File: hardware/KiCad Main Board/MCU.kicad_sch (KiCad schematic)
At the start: 41 parts, among them J1 SWD Debug, J2 USB_C_Receptacle_USB2.0_14P, U1 W25Q128JVS, U7 RP2350B-QFN80, Y1 ABM8-272-T3

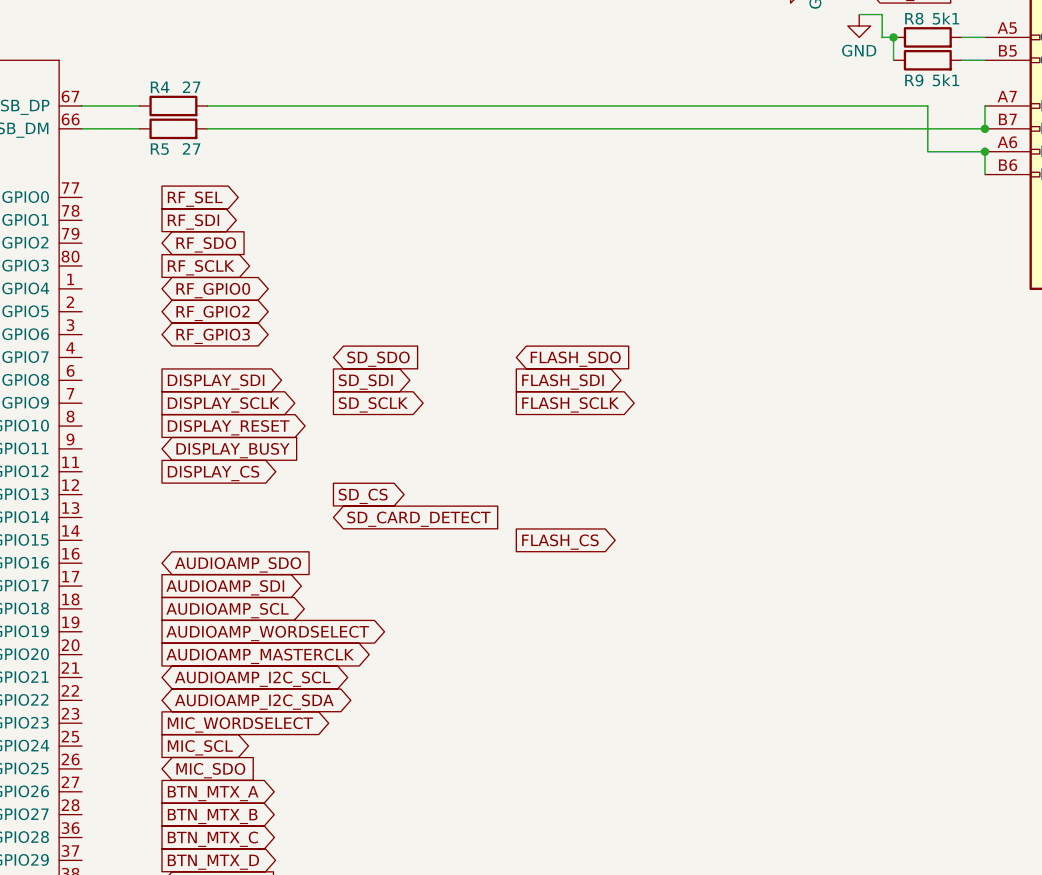
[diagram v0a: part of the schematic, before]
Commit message: added connector for RF daughter board
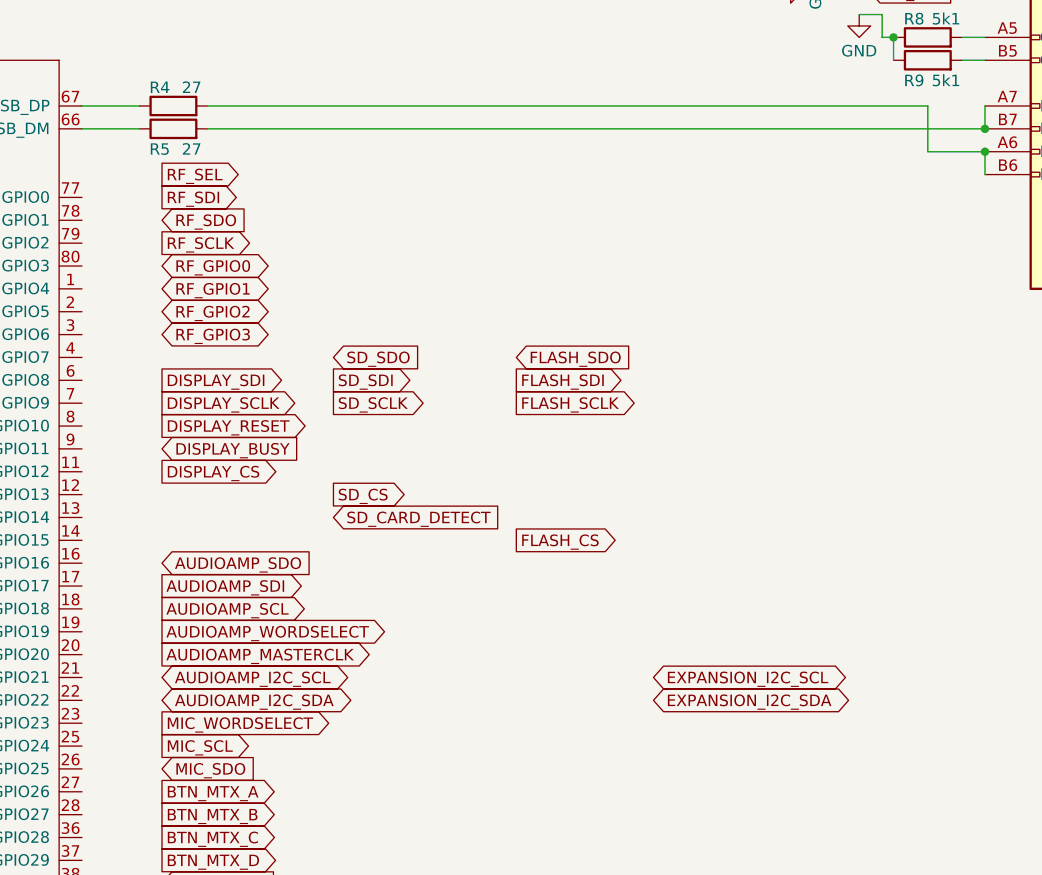
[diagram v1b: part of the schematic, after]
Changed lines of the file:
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@@
 				)
 			)
-			(table_cell "CC1120 (RF IC), Wisblock GPS/Expansions"
+			(table_cell "CC1120 (RF IC), Expansion"
 				(exclude_from_sim no)
 				(at 218.44 143.51 0)
@@
 				)
 			)
-			(table_cell "Audio IC, Wisblock GPS/Expansions"
+			(table_cell "Audio IC, Expansion"
 				(exclude_from_sim no)
 				(at 218.44 148.59 0)
@@
 		)
 	)
+	(global_label "RF_GPIO1"
+		(shape bidirectional)
+		(at 156.21 63.5 0)
+		(fields_autoplaced yes)
+		(effects
+			(font
+				(size 1.27 1.27)
+			)
+			(justify left)
+		)
+		(property "Intersheetrefs" "${INTERSHEET_REFS}"
+			(at 169.3175 63.5 0)
+			(effects
+				(font
+					(size 1.27 1.27)
+				)
+				(justify left)
+				(hide yes)
+			)
+		)
+	)
 	(global_label "BTN_MTX_3"
 		(shape input)
@@
 	(global_label "RF_SDO"
 		(shape input)
-		(at 156.21 58.42 0)
-		(fields_autoplaced yes)
-		(effects
-			(font
-				(size 1.27 1.27)
-			)
-			(justify left)
-		)
-		(property "Intersheetrefs" "${INTERSHEET_REFS}"
-			(at 166.3314 58.42 0)
+		(at 156.21 55.88 0)
+		(fields_autoplaced yes)
+		(effects
+			(font
+				(size 1.27 1.27)
+			)
+			(justify left)
+		)
+		(property "Intersheetrefs" "${INTERSHEET_REFS}"
+			(at 166.3314 55.88 0)
 			(effects
 				(font
@@
 		)
 	)
+	(global_label "EXPANSION_I2C_SCL"
+		(shape bidirectional)
+		(at 210.82 106.68 0)
+		(fields_autoplaced yes)
+		(effects
+			(font
+				(size 1.27 1.27)
+			)
+			(justify left)
+		)
+		(property "Intersheetrefs" "${INTERSHEET_REFS}"
+			(at 233.9665 106.68 0)
+			(effects
+				(font
+					(size 1.27 1.27)
+				)
+				(justify left)
+				(hide yes)
+			)
+		)
+	)
 	(global_label "BTN_ENC_B"
 		(shape input)
@@
 	(global_label "RF_SDI"
 		(shape output)
-		(at 156.21 55.88 0)
-		(fields_autoplaced yes)
-		(effects
-			(font
-				(size 1.27 1.27)
-			)
-			(justify left)
-		)
-		(property "Intersheetrefs" "${INTERSHEET_REFS}"
-			(at 165.6057 55.88 0)
+		(at 156.21 53.34 0)
+		(fields_autoplaced yes)
+		(effects
+			(font
+				(size 1.27 1.27)
+			)
+			(justify left)
+		)
+		(property "Intersheetrefs" "${INTERSHEET_REFS}"
+			(at 165.6057 53.34 0)
 			(effects
 				(font
@@
 	(global_label "RF_SEL"
 		(shape output)
-		(at 156.21 53.34 0)
-		(fields_autoplaced yes)
-		(effects
-			(font
-				(size 1.27 1.27)
-			)
-			(justify left)
-		)
-		(property "Intersheetrefs" "${INTERSHEET_REFS}"
-			(at 165.908 53.34 0)
+		(at 156.21 50.8 0)
+		(fields_autoplaced yes)
+		(effects
+			(font
+				(size 1.27 1.27)
+			)
+			(justify left)
+		)
+		(property "Intersheetrefs" "${INTERSHEET_REFS}"
+			(at 165.908 50.8 0)
 			(effects
 				(font
@@
 	(global_label "RF_GPIO0"
 		(shape bidirectional)
-		(at 156.21 63.5 0)
-		(fields_autoplaced yes)
-		(effects
-			(font
-				(size 1.27 1.27)
-			)
-			(justify left)
-		)
-		(property "Intersheetrefs" "${INTERSHEET_REFS}"
-			(at 169.3175 63.5 0)
+		(at 156.21 60.96 0)
+		(fields_autoplaced yes)
+		(effects
+			(font
+				(size 1.27 1.27)
+			)
+			(justify left)
+		)
+		(property "Intersheetrefs" "${INTERSHEET_REFS}"
+			(at 169.3175 60.96 0)
 			(effects
 				(font
@@
 		)
 	)
+	(global_label "EXPANSION_I2C_SDA"
+		(shape bidirectional)
+		(at 210.82 109.22 0)
+		(fields_autoplaced yes)
+		(effects
+			(font
+				(size 1.27 1.27)
+			)
+			(justify left)
+		)
+		(property "Intersheetrefs" "${INTERSHEET_REFS}"
+			(at 234.027 109.22 0)
+			(effects
+				(font
+					(size 1.27 1.27)
+				)
+				(justify left)
+				(hide yes)
+			)
+		)
+	)
 	(global_label "AUDIOAMP_SCL"
 		(shape output)
@@
 	(global_label "RF_SCLK"
 		(shape output)
-		(at 156.21 60.96 0)
-		(fields_autoplaced yes)
-		(effects
-			(font
-				(size 1.27 1.27)
-			)
-			(justify left)
-		)
-		(property "Intersheetrefs" "${INTERSHEET_REFS}"
-			(at 167.299 60.96 0)
-			(effects
-				(font
+		(at 156.21 58.42 0)
+		(fields_autoplaced yes)
+		(effects
+			(font
+				(size 1.27 1.27)
+			)
+			(justify left)
+		)
+		(property "Intersheetrefs" "${INTERSHEET_REFS}"
+			(at 167.299 58.42 0)
+			(effects
+				(font
